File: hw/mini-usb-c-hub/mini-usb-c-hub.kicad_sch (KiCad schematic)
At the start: 29 parts, among them J101 USB_C_Receptacle_USB2.0_16P, P101 USB_C_Plug_USB3.0, U101 FE1.1s, Y101 12MHz

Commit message: chore(hw): lay-out some differential pairs
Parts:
- renumbered C1 to C101, C104 to C102, C102 to C104, C101 to C105, C2 to C106, C3 to C107, C105 to C108, C106 to C109, D109 to D103, D108 to D104, R1 to R101, R2 to R102, R101 to R103, R3 to R104, R106 to R105, R103 to R106, R104 to R108, R105 to R109, R109 to R110, R102 to R111, R108 to R112
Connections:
- net D1USB+: now also D102.2 (I/O1); no longer D102.3 (I/O2)
- net D1USB-: now also D102.3 (I/O2); no longer D102.2 (I/O1)
- net UUSB+: now also D101.2 (I/O1); no longer D101.3 (I/O2)
- net UUSB-: now also D101.3 (I/O2); no longer D101.2 (I/O1)
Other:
- moved on the sheet: C102, C103, C104, C105, C106, C107, D103, D104, R104, R105, R106, R108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

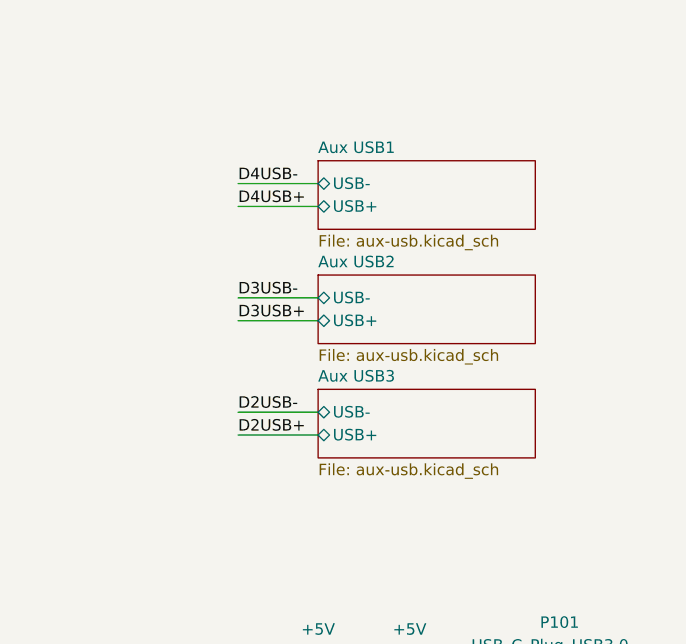
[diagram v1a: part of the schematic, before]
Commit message: chore(hw): attempt to layout without one USB A
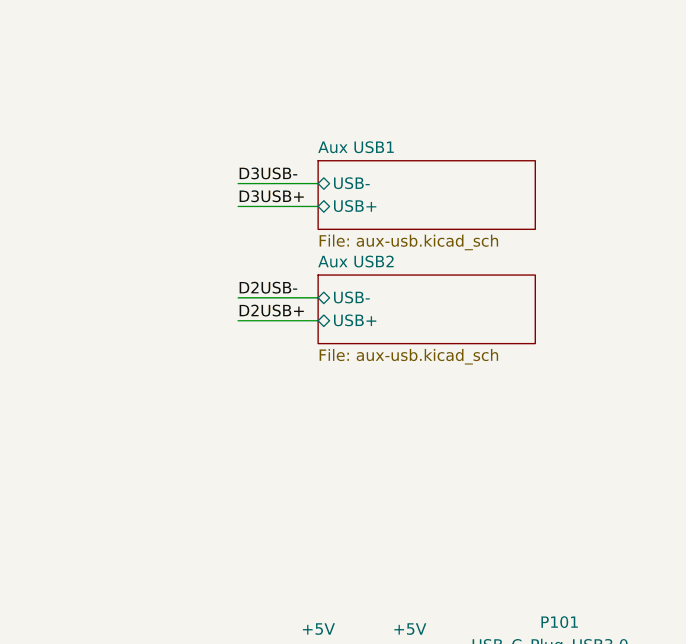
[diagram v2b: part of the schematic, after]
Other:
- removed sheet Aux USB3
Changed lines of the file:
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@@
 	(wire
 		(pts
-			(xy 231.14 55.88) (xy 240.03 55.88)
+			(xy 231.14 43.18) (xy 240.03 43.18)
 		)
 		(stroke
@@
 	(wire
 		(pts
-			(xy 231.14 43.18) (xy 240.03 43.18)
-		)
-		(stroke
-			(width 0)
-			(type default)
-		)
-	)
-	(wire
-		(pts
 			(xy 160.02 134.62) (xy 160.02 140.97)
 		)
@@
 	(wire
 		(pts
-			(xy 231.14 53.34) (xy 240.03 53.34)
+			(xy 231.14 40.64) (xy 240.03 40.64)
 		)
 		(stroke
@@
 	(wire
 		(pts
-			(xy 231.14 66.04) (xy 240.03 66.04)
+			(xy 231.14 53.34) (xy 240.03 53.34)
 		)
 		(stroke
@@
 	(wire
 		(pts
-			(xy 231.14 40.64) (xy 240.03 40.64)
-		)
-		(stroke
-			(width 0)
-			(type default)
-		)
-	)
-	(wire
-		(pts
 			(xy 156.21 104.14) (xy 166.37 104.14)
 		)
@@
 	(wire
 		(pts
-			(xy 231.14 68.58) (xy 240.03 68.58)
+			(xy 231.14 55.88) (xy 240.03 55.88)
 		)
 		(stroke
@@
 	)
 	(label "D2USB-"
-		(at 231.14 66.04 0)
+		(at 231.14 53.34 0)
 		(fields_autoplaced yes)
 		(effects
@@
 	)
 	(label "D3USB+"
-		(at 231.14 55.88 0)
-		(fields_autoplaced yes)
-		(effects
-			(font
-				(size 1.27 1.27)
-			)
-			(justify left bottom)
-		)
-	)
-	(label "D4USB+"
 		(at 231.14 43.18 0)
 		(fields_autoplaced yes)
@@
 	)
 	(label "D2USB+"
-		(at 231.14 68.58 0)
+		(at 231.14 55.88 0)
 		(fields_autoplaced yes)
 		(effects
@@
 		)
 	)
-	(label "D4USB-"
-		(at 231.14 40.64 0)
-		(fields_autoplaced yes)
-		(effects
-			(font
-				(size 1.27 1.27)
-			)
-			(justify left bottom)
-		)
-	)
 	(label "D3USB-"
-		(at 231.14 53.34 0)
+		(at 231.14 40.64 0)
 		(fields_autoplaced yes)
 		(effects
@@
 				)
 			)
-		)
-	)
-	(sheet
-		(at 240.03 63.5)
-		(size 24.13 7.62)
-		(fields_autoplaced yes)
-		(stroke
-			(width 0.1524)
-			(type solid)
-		)
-		(fill
-			(color 0 0 0 0.0000)
-		)
-		(property "Sheetname" "Aux USB3"
-			(at 240.03 62.7884 0)
-			(effects
-				(font
-					(size 1.27 1.27)
-				)
-				(justify left bottom)
-			)
-		)
-		(property "Sheetfile" "aux-usb.kicad_sch"
-			(at 240.03 71.7046 0)
-			(effects
-				(font
-					(size 1.27 1.27)
-				)
-				(justify left top)
-			)
-		)
-		(pin "USB+" bidirectional
-			(at 240.03 68.58 180)
-			(effects
-				(font
-					(size 1.27 1.27)
-				)
-				(justify left)
-			)
-		)
-		(pin "USB-" bidirectional
-			(at 240.03 66.04 180)
-			(effects
-				(font
-					(size 1.27 1.27)
-				)
-				(justify left)
-			)
-		)
-		(instances
-			(project "mini-usb-c-hub"
-				(path "/7c04e056-0d84-4da3-ae50-c0eef25c6fa4"
-					(page "5")
-				)
-			)

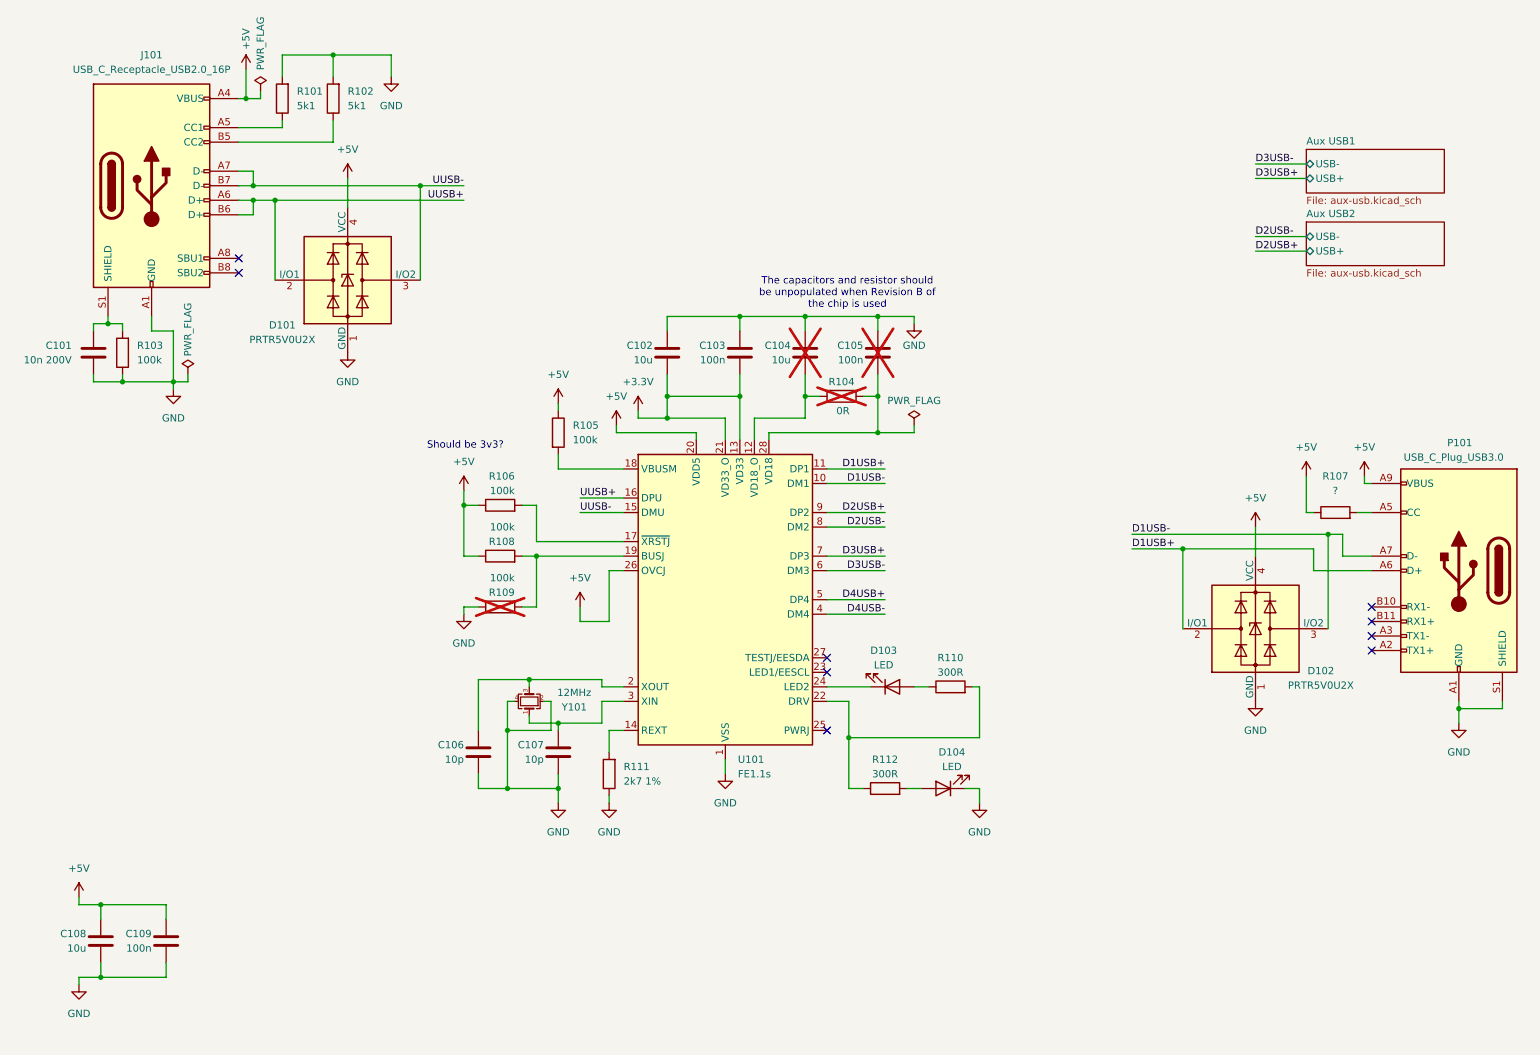
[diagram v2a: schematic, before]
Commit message: chore(hw): layout support components
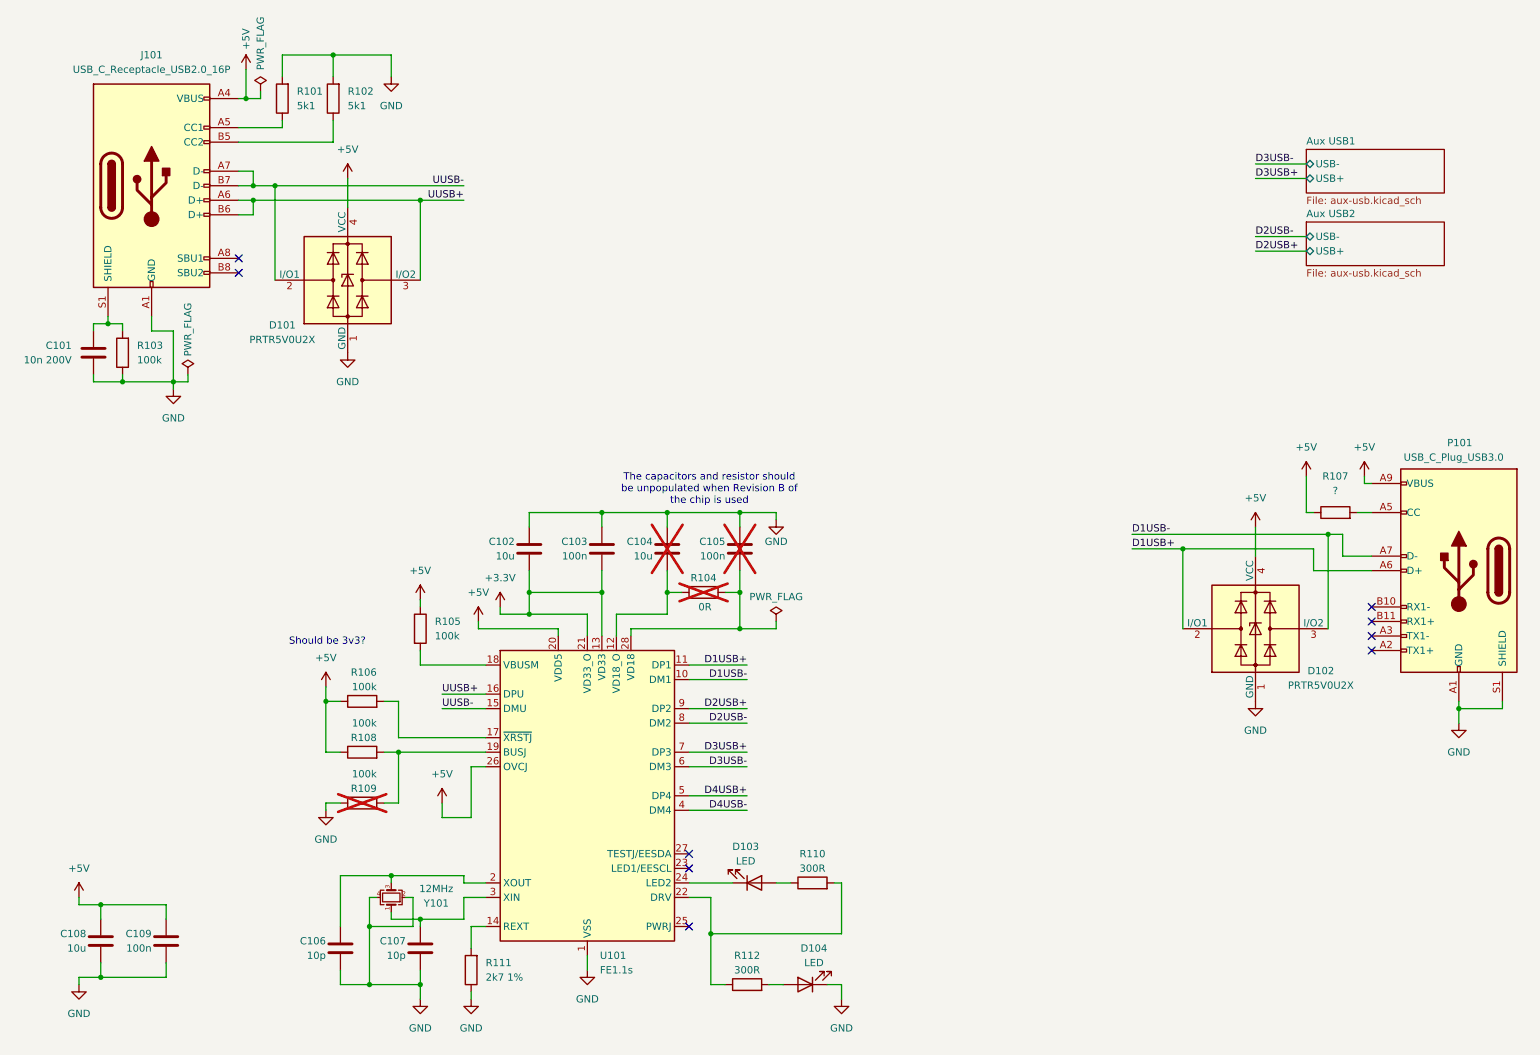
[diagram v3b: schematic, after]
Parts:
- C106, C107: footprint Capacitor_SMD:C_1206_3216Metric_Pad1.33x1.80mm_HandSolder -> Capacitor_SMD:C_0805_2012Metric_Pad1.18x1.45mm_HandSolder
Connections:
- net UUSB+: now also D101.3 (I/O2); no longer D101.2 (I/O1)
- net UUSB-: now also D101.2 (I/O1); no longer D101.3 (I/O2)
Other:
- moved on the sheet: C102, C103, C104, C105, C106, C107, D103, D104, R104, R105, R106, R108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

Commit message: chore(hw): layout around switch and add downstream USB-C
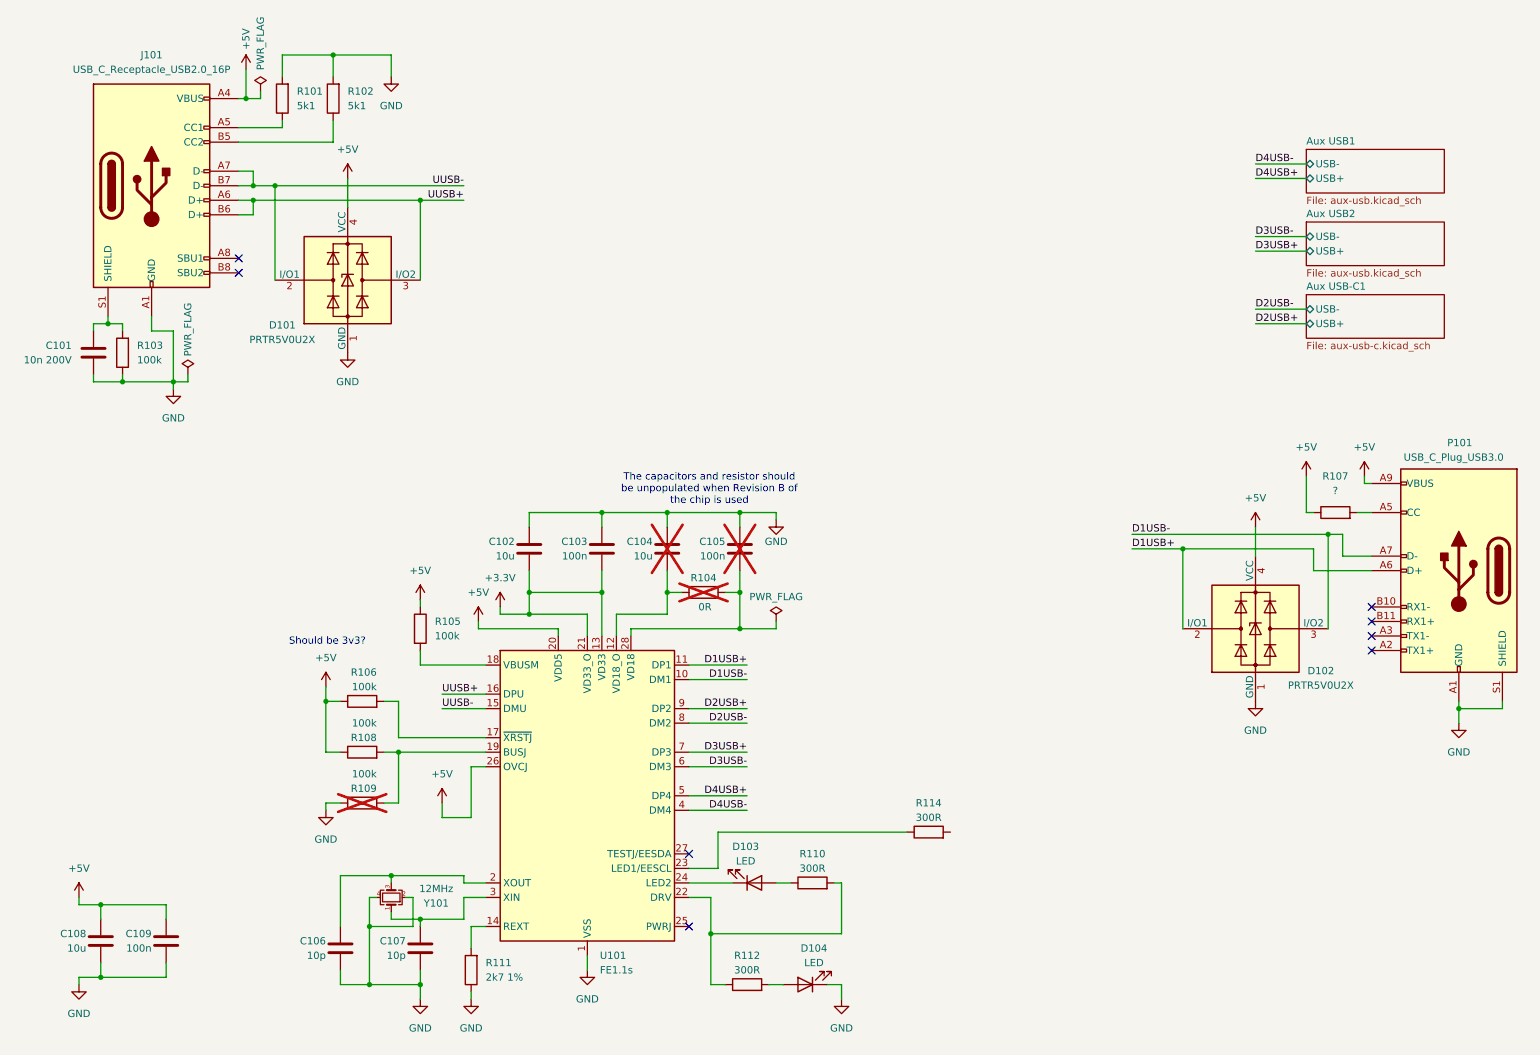
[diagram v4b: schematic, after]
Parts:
- added R114: 300R, Resistor_SMD:R_0805_2012Metric_Pad1.20x1.40mm_HandSolder, symbol Device:R
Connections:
- net at U101.23 (LED1/EESCL): now also R114.1
- no-connect marks 9 -> 8
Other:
- added sheet Aux USB-C1 (aux-usb-c.kicad_sch)
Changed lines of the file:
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@@
 	)
 	(no_connect
-		(at 53.34 57.15)
+		(at 132.08 161.29)
 	)
 	(no_connect
-		(at 53.34 59.69)
+		(at 53.34 57.15)
 	)
 	(no_connect
-		(at 132.08 163.83)
+		(at 53.34 59.69)
 	)
 	(no_connect
@@
 	)
 	(no_connect
-		(at 132.08 161.29)
-	)
-	(no_connect
 		(at 251.46 118.11)
 	)
@@
 	(wire
 		(pts
-			(xy 231.14 43.18) (xy 240.03 43.18)
+			(xy 231.14 55.88) (xy 240.03 55.88)
 		)
 		(stroke
@@
 	(wire
 		(pts
+			(xy 137.16 157.48) (xy 170.18 157.48)
+		)
+		(stroke
+			(width 0)
+			(type default)
+		)
+	)
+	(wire
+		(pts
 			(xy 266.7 134.62) (xy 266.7 135.89)
 		)
@@
 	(wire
 		(pts
+			(xy 137.16 163.83) (xy 137.16 157.48)
+		)
+		(stroke
+			(width 0)
+			(type default)
+		)
+	)
+	(wire
+		(pts
 			(xy 30.48 67.31) (xy 30.48 68.58)
 		)
@@
 	(wire
 		(pts
-			(xy 231.14 40.64) (xy 240.03 40.64)
+			(xy 231.14 53.34) (xy 240.03 53.34)
 		)
 		(stroke
@@
 	(wire
 		(pts
+			(xy 132.08 163.83) (xy 137.16 163.83)
+		)
+		(stroke
+			(width 0)
+			(type default)
+		)
+	)
+	(wire
+		(pts
 			(xy 158.75 166.37) (xy 157.48 166.37)
 		)
@@
 	(wire
 		(pts
+			(xy 231.14 40.64) (xy 240.03 40.64)
+		)
+		(stroke
+			(width 0)
+			(type default)
+		)
+	)
+	(wire
+		(pts
 			(xy 68.58 132.08) (xy 68.58 134.62)
 		)
@@
 	(wire
 		(pts
-			(xy 231.14 53.34) (xy 240.03 53.34)
+			(xy 231.14 66.04) (xy 240.03 66.04)
 		)
 		(stroke
@@
 	(wire
 		(pts
-			(xy 231.14 55.88) (xy 240.03 55.88)
+			(xy 231.14 43.18) (xy 240.03 43.18)
+		)
+		(stroke
+			(width 0)
+			(type default)
+		)
+	)
+	(wire
+		(pts
+			(xy 231.14 68.58) (xy 240.03 68.58)
 		)
 		(stroke
@@
 	)
 	(label "D2USB-"
-		(at 231.14 53.34 0)
+		(at 231.14 66.04 0)
 		(fields_autoplaced yes)
 		(effects
@@
 		)
 	)
+	(label "D4USB+"
+		(at 231.14 43.18 0)
+		(fields_autoplaced yes)
+		(effects
+			(font
+				(size 1.27 1.27)
+			)
+			(justify left bottom)
+		)
+	)
 	(label "D1USB+"
 		(at 209.55 107.95 0)
@@
 	)
 	(label "D3USB+"
-		(at 231.14 43.18 0)
+		(at 231.14 55.88 0)
 		(fields_autoplaced yes)
 		(effects
@@
 		)
 	)
+	(label "D4USB-"
+		(at 231.14 40.64 0)
+		(fields_autoplaced yes)
+		(effects
+			(font
+				(size 1.27 1.27)
+			)
+			(justify left bottom)
+		)
+	)
 	(label "D4USB+"
 		(at 142.24 151.13 180)
@@
 	)
 	(label "D2USB+"
-		(at 231.14 55.88 0)
+		(at 231.14 68.58 0)
 		(fields_autoplaced yes)
 		(effects
@@
 	)
 	(label "D3USB-"
-		(at 231.14 40.64 0)
+		(at 231.14 53.34 0)
 		(fields_autoplaced yes)
 		(effects
@@
 	)
 	(symbol
+		(lib_id "Device:R")
+		(at 173.99 157.48 90)
+		(unit 1)
+		(exclude_from_sim no)
+		(in_bom yes)
+		(on_board yes)
+		(dnp no)
+		(property "Reference" "R114"
+			(at 173.99 152.4 90)
+			(effects
+				(font
+					(size 1.27 1.27)
+				)
+			)
+		)
+		(property "Value" "300R"
+			(at 173.99 154.94 90)
+			(effects
+				(font
+					(size 1.27 1.27)
+				)
+			)
+		)
+		(property "Footprint" "Resistor_SMD:R_0805_2012Metric_Pad1.20x1.40mm_HandSolder"
+			(at 173.99 159.258 90)
+			(effects
+				(font
+					(size 1.27 1.27)
+				)
+				(hide yes)
+			)
+		)
+		(property "Datasheet" "~"
+			(at 173.99 157.48 0)
+			(effects
+				(font
+					(size 1.27 1.27)
+				)
+				(hide yes)
+			)
+		)
+		(property "Description" "Resistor"
+			(at 173.99 157.48 0)
+			(effects
+				(font
+					(size 1.27 1.27)
+				)
+				(hide yes)
+			)
+		)
+		(pin "2"
+		)
+		(pin "1"
+		)
+		(instances
+			(project "mini-usb-c-hub"
+				(path "/7c04e056-0d84-4da3-ae50-c0eef25c6fa4"
+					(reference "R114")
+					(unit 1)
+				)
+			)
+		)
+	)
+	(symbol
 		(lib_id "Power_Protection:PRTR5V0U2X")
 		(at 231.14 121.92 0)
@@
 			(effects
 				(font
+					(size 1.27 1.27)
+				)
+				(justify left)
+			)
+		)
+		(instances
+			(project "mini-usb-c-hub"
+				(path "/7c04e056-0d84-4da3-ae50-c0eef25c6fa4"
+					(page "4")
+				)
+			)
+		)
+	)
+	(sheet
+		(at 240.03 63.5)
+		(size 24.13 7.62)
+		(fields_autoplaced yes)
+		(stroke
+			(width 0.1524)
+			(type solid)
+		)
+		(fill
+			(color 0 0 0 0.0000)
+		)
+		(property "Sheetname" "Aux USB-C1"
+			(at 240.03 62.7884 0)
+			(effects
+				(font
+					(size 1.27 1.27)
+				)
+				(justify left bottom)
+			)
+		)
+		(property "Sheetfile" "aux-usb-c.kicad_sch"
+			(at 240.03 71.7046 0)
+			(effects
+				(font
+					(size 1.27 1.27)
+				)
+				(justify left top)
+			)
+		)
+		(pin "USB+" bidirectional
+			(at 240.03 68.58 180)
+			(effects
+				(font
+					(size 1.27 1.27)
+				)
+				(justify left)
+			)
+		)
+		(pin "USB-" bidirectional
+			(at 240.03 66.04 180)
+			(effects
+				(font
